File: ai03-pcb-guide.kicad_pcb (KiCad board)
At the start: 2 copper layers, 76.2 x 38.1 mm, 24 parts, among them SW1 SW_Push, U1 ATmega32U4-AU, Y1 16MHz

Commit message: Generate gerbers
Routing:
- added copper zone on B.Cu, net GND
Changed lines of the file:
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@@
   (segment (start 66.487 86.553) (end 68.199 86.553) (width 0.254) (layer B.Cu) (net 28))
   (segment (start 66.23 86.296) (end 66.487 86.553) (width 0.254) (layer B.Cu) (net 28))
+  (zone (net 2) (net_name GND) (layer B.Cu) (hatch edge 0.508)
+    (connect_pads (clearance 0.508))
+    (min_thickness 0.254)
+    (fill yes (arc_segments 16) (thermal_gap 0.508) (thermal_bridge_width 0.508))
+    (polygon
+      (pts
+        (xy 35.71875 69.05625) (xy 43.65625 69.05625) (xy 43.65625 61.9125) (xy 35.71875 61.9125)
+      )
+    )
+  )
+  (zone (net 2) (net_name GND) (layer B.Cu) (hatch edge 0.508)
+    (connect_pads (clearance 0.508))
+    (min_thickness 0.254)
+    (fill yes (arc_segments 16) (thermal_gap 0.508) (thermal_bridge_width 0.508))
+    (polygon
+      (pts
+        (xy 50.8 65.0875) (xy 66.675 65.0875) (xy 66.675 75.40625) (xy 50.8 75.40625)
+      )
+    )
+  )
+  (zone (net 2) (net_name GND) (layer B.Cu) (hatch edge 0.508)
+    (connect_pads (clearance 0.508))
+    (min_thickness 0.254)
+    (fill yes (arc_segments 16) (thermal_gap 0.508) (thermal_bridge_width 0.508))
+    (polygon
+      (pts
+        (xy 53.975 77.7875) (xy 63.5 77.7875) (xy 63.5 87.3125) (xy 53.975 87.3125)
+      )
+    )
+  )
 )

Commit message: Generate BOM
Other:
- board text added: "Hello World!"
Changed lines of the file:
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@@
   (general
     (thickness 1.6)
-    (drawings 8)
+    (drawings 9)
     (tracks 210)
     (zones 0)
@@
     (visible_elements FFFFFF7F)
     (pcbplotparams
-      (layerselection 0x010fc_ffffffff)
-      (usegerberextensions false)
+      (layerselection 0x010f0_ffffffff)
+      (usegerberextensions true)
       (usegerberattributes false)
       (usegerberadvancedattributes false)
@@
       (plotinvisibletext false)
       (padsonsilk false)
-      (subtractmaskfromsilk false)
+      (subtractmaskfromsilk true)
       (outputformat 1)
       (mirror false)
-      (drillshape 1)
+      (drillshape 0)
       (scaleselection 1)
-      (outputdirectory ""))
+      (outputdirectory "Gerbers"))
   )
   (net 0 "")
@@
     )
   )
+  (gr_text "Hello World!" (at 40.48125 97.63125) (layer F.SilkS)
+    (effects (font (size 1.5 1.5) (thickness 0.3)))
+  )
   (gr_arc (start 105.56875 64.29375) (end 107.95 64.29375) (angle -90) (layer Edge.Cuts) (width 0.2))

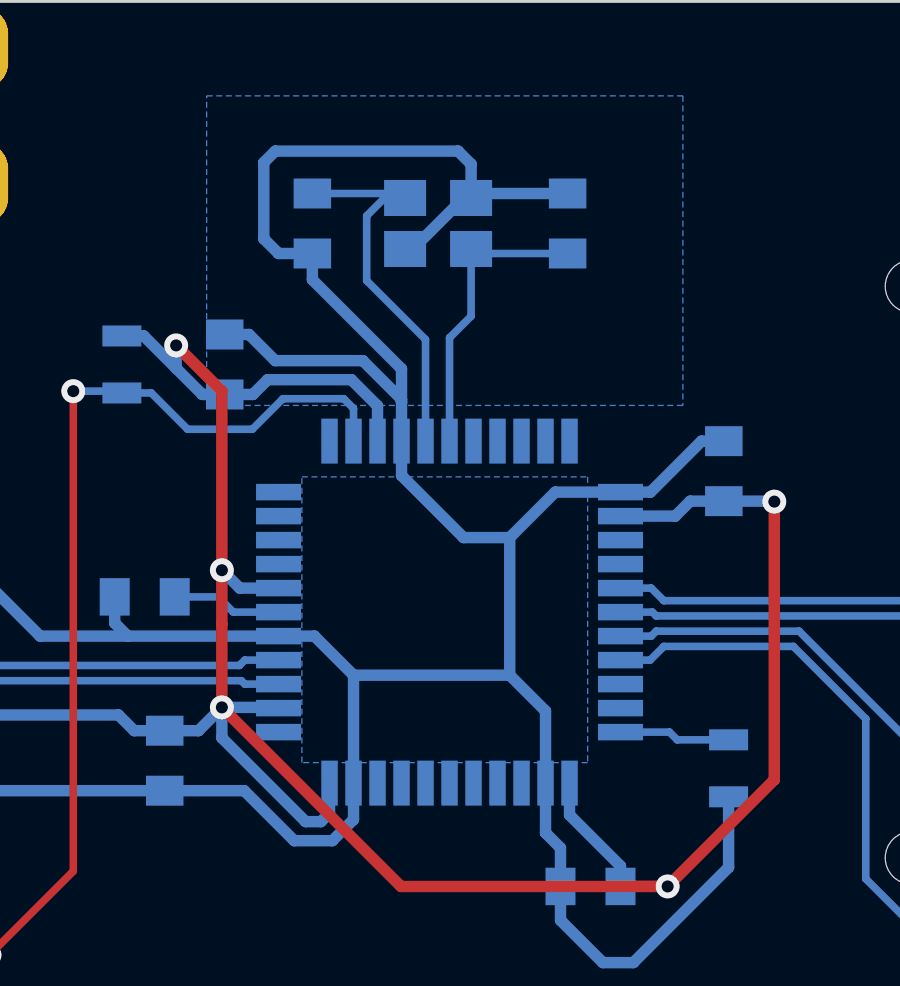
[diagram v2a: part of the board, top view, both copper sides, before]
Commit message: Update PCB for revised guide
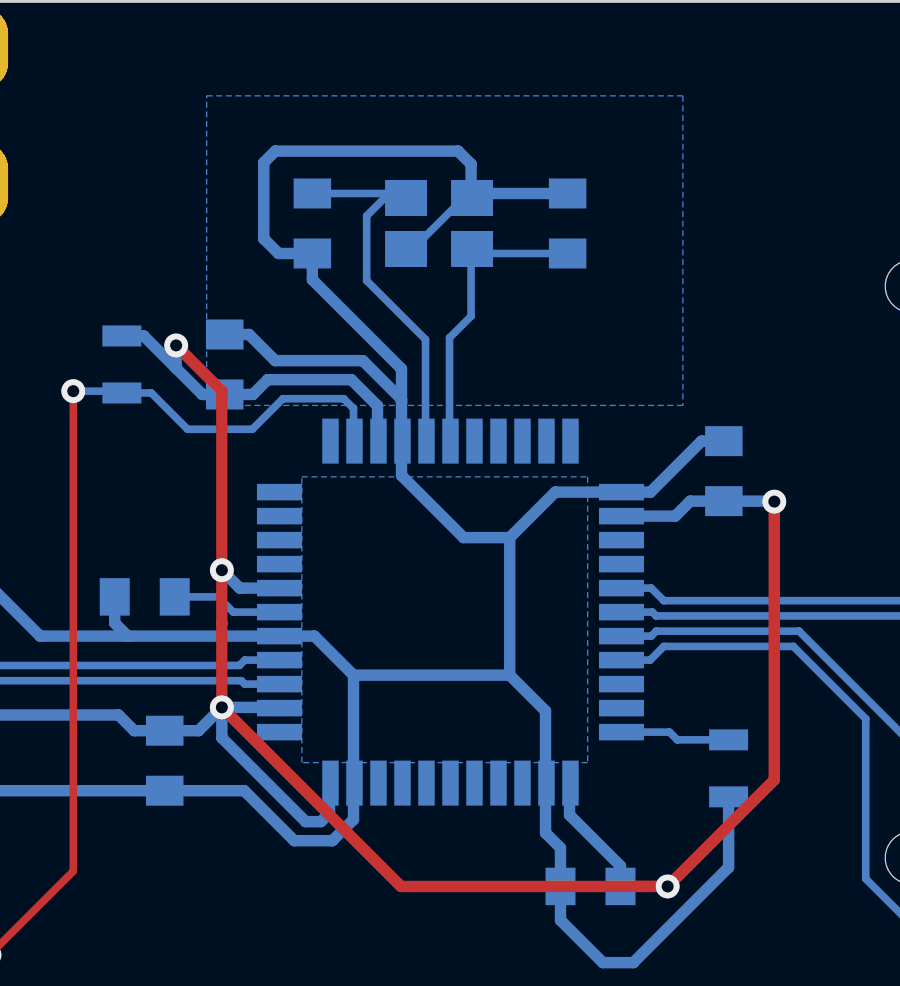
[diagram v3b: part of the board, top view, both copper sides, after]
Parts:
- MX1, MX2, MX3, MX4: value MX-1U -> MX-NoLED
- Y1: value 16MHz -> Crystal_GND24_Small
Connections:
- MX1 pad 3: Net-(MX1-Pad3) -> (no net)
- MX1 pad 4: Net-(MX1-Pad4) -> (no net)
- MX2 pad 3: Net-(MX2-Pad3) -> (no net)
- MX2 pad 4: Net-(MX2-Pad4) -> (no net)
- MX3 pad 3: Net-(MX3-Pad3) -> (no net)
- MX3 pad 4: Net-(MX3-Pad4) -> (no net)
- MX4 pad 3: Net-(MX4-Pad3) -> (no net)
- MX4 pad 4: Net-(MX4-Pad4) -> (no net)
